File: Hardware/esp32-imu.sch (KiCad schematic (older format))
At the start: 14 parts, among them SW1 SW_MEC_5E, SW2 SW_MEC_5E

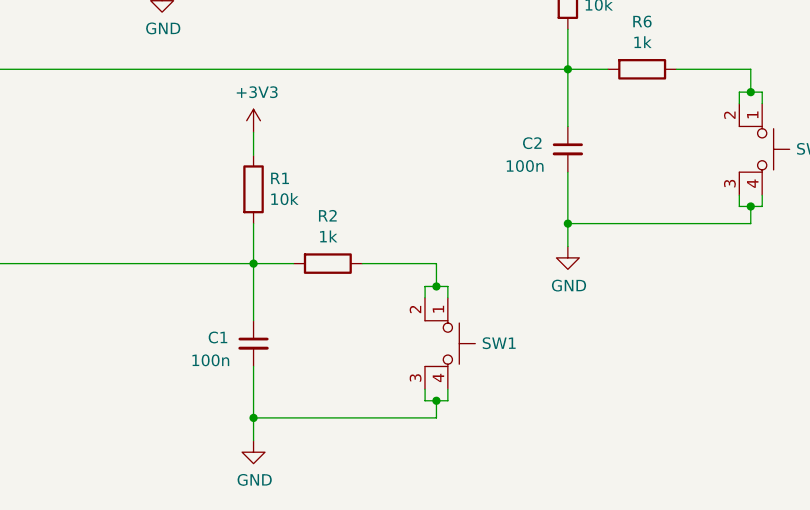
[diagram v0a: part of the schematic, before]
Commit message: Version with SMDs for externa external manufacturing
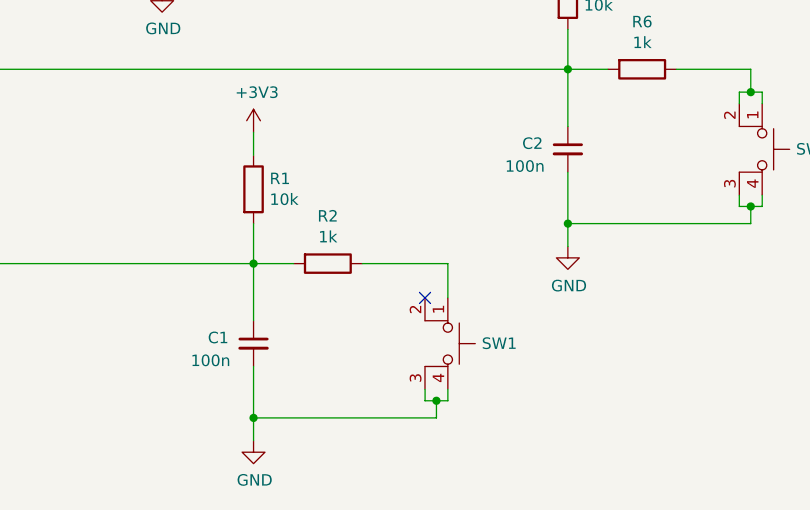
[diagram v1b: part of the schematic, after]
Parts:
- C1, C2, C3: footprint Capacitor_THT:C_Disc_D5.0mm_W2.5mm_P5.00mm -> Capacitor_SMD:C_0805_2012Metric_Pad1.18x1.45mm_HandSolder
- R1, R2, R3, R4, R5, R6: footprint Resistor_THT:R_Axial_DIN0207_L6.3mm_D2.5mm_P10.16mm_Horizontal -> Resistor_SMD:R_0805_2012Metric_Pad1.20x1.40mm_HandSolder
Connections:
- net at R2.1, SW1.1: no longer SW1.2
- no-connect marks 5 -> 6
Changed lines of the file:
@@
 Sheet 1 1
 Title "ESP32 + IMU"
-Date "2021-10-04"
-Rev "v0.1.0"
+Date "2021-10-12"
+Rev "v0.2.0"
 Comp "Universitat de Barcelona"
 Comment1 "Repo: https://github.com/TheAlbertDev/pcb-esp32-imu"
@@
 F 0 "R3" H 6720 2046 50  0000 L CNN
 F 1 "2k2" H 6720 1955 50  0000 L CNN
-F 2 "Resistor_THT:R_Axial_DIN0207_L6.3mm_D2.5mm_P10.16mm_Horizontal" V 6580 2000 50  0001 C CNN
+F 2 "Resistor_SMD:R_0805_2012Metric_Pad1.20x1.40mm_HandSolder" V 6580 2000 50  0001 C CNN
 F 3 "~" H 6650 2000 50  0001 C CNN
 	1    6650 2000
@@
 F 0 "R5" H 7195 2046 50  0000 L CNN
 F 1 "2k2" H 7195 1955 50  0000 L CNN
-F 2 "Resistor_THT:R_Axial_DIN0207_L6.3mm_D2.5mm_P10.16mm_Horizontal" V 7055 2000 50  0001 C CNN
+F 2 "Resistor_SMD:R_0805_2012Metric_Pad1.20x1.40mm_HandSolder" V 7055 2000 50  0001 C CNN
 F 3 "~" H 7125 2000 50  0001 C CNN
 	1    7125 2000
@@
 F 0 "C3" H 8225 2100 50  0000 R CNN
 F 1 "100n" H 8300 2000 50  0000 R CNN
-F 2 "Capacitor_THT:C_Disc_D5.0mm_W2.5mm_P5.00mm" H 8025 2075 50  0001 C CNN
+F 2 "Capacitor_SMD:C_0805_2012Metric_Pad1.18x1.45mm_HandSolder" H 8025 2075 50  0001 C CNN
 F 3 "~" H 8025 2075 50  0001 C CNN
 	1    8025 2075
@@
 F 0 "R4" H 6945 3921 50  0000 L CNN
 F 1 "10k" H 6945 3830 50  0000 L CNN
-F 2 "Resistor_THT:R_Axial_DIN0207_L6.3mm_D2.5mm_P10.16mm_Horizontal" V 6805 3875 50  0001 C CNN
+F 2 "Resistor_SMD:R_0805_2012Metric_Pad1.20x1.40mm_HandSolder" V 6805 3875 50  0001 C CNN
 F 3 "~" H 6875 3875 50  0001 C CNN
 	1    6875 3875
@@
 F 0 "R6" V 6993 4200 50  0000 C CNN
 F 1 "1k" V 7084 4200 50  0000 C CNN
-F 2 "Resistor_THT:R_Axial_DIN0207_L6.3mm_D2.5mm_P10.16mm_Horizontal" V 7130 4200 50  0001 C CNN
+F 2 "Resistor_SMD:R_0805_2012Metric_Pad1.20x1.40mm_HandSolder" V 7130 4200 50  0001 C CNN
 F 3 "~" H 7200 4200 50  0001 C CNN
 	1    7200 4200
@@
 F 0 "C2" H 7075 4575 50  0000 R CNN
 F 1 "100n" H 7150 4475 50  0000 R CNN
-F 2 "Capacitor_THT:C_Disc_D5.0mm_W2.5mm_P5.00mm" H 6875 4550 50  0001 C CNN
+F 2 "Capacitor_SMD:C_0805_2012Metric_Pad1.18x1.45mm_HandSolder" H 6875 4550 50  0001 C CNN
 F 3 "~" H 6875 4550 50  0001 C CNN
 	1    6875 4550
@@
 F 0 "R1" H 5570 4771 50  0000 L CNN
 F 1 "10k" H 5570 4680 50  0000 L CNN
-F 2 "Resistor_THT:R_Axial_DIN0207_L6.3mm_D2.5mm_P10.16mm_Horizontal" V 5430 4725 50  0001 C CNN
+F 2 "Resistor_SMD:R_0805_2012Metric_Pad1.20x1.40mm_HandSolder" V 5430 4725 50  0001 C CNN
 F 3 "~" H 5500 4725 50  0001 C CNN
 	1    5500 4725
@@
 F 0 "R2" V 5618 5050 50  0000 C CNN
 F 1 "1k" V 5709 5050 50  0000 C CNN
-F 2 "Resistor_THT:R_Axial_DIN0207_L6.3mm_D2.5mm_P10.16mm_Horizontal" V 5755 5050 50  0001 C CNN
+F 2 "Resistor_SMD:R_0805_2012Metric_Pad1.20x1.40mm_HandSolder" V 5755 5050 50  0001 C CNN
 F 3 "~" H 5825 5050 50  0001 C CNN
 	1    5825 5050
@@
 $EndComp
 Wire Wire Line
-	5975 5050 6300 5050
-Wire Wire Line
-	6300 5050 6300 5150
-Wire Wire Line
-	6300 5150 6350 5150
-Wire Wire Line
-	6350 5150 6350 5200
-Wire Wire Line
-	6250 5150 6300 5150
-Connection ~ 6300 5150
-Wire Wire Line
-	6250 5150 6250 5200
+	5975 5050 6350 5050
 $Comp
 L Device:C_Small C1
@@
 F 0 "C1" H 5700 5425 50  0000 R CNN
 F 1 "100n" H 5775 5325 50  0000 R CNN
-F 2 "Capacitor_THT:C_Disc_D5.0mm_W2.5mm_P5.00mm" H 5500 5400 50  0001 C CNN
+F 2 "Capacitor_SMD:C_0805_2012Metric_Pad1.18x1.45mm_HandSolder" H 5500 5400 50  0001 C CNN
 F 3 "~" H 5500 5400 50  0001 C CNN
 	1    5500 5400
@@
 Wire Wire Line
 	4100 5050 5500 5050
+NoConn ~ 6250 5200
+Wire Wire Line
+	6350 5050 6350 5200
 $EndSCHEMATC
